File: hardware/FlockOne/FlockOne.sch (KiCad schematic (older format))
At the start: 13 parts, among them J1 Port, J2 Programming, U1 MIC5219-3.3YM5, U2 STM32F030F4P6, U3 AITHINKER-RA02

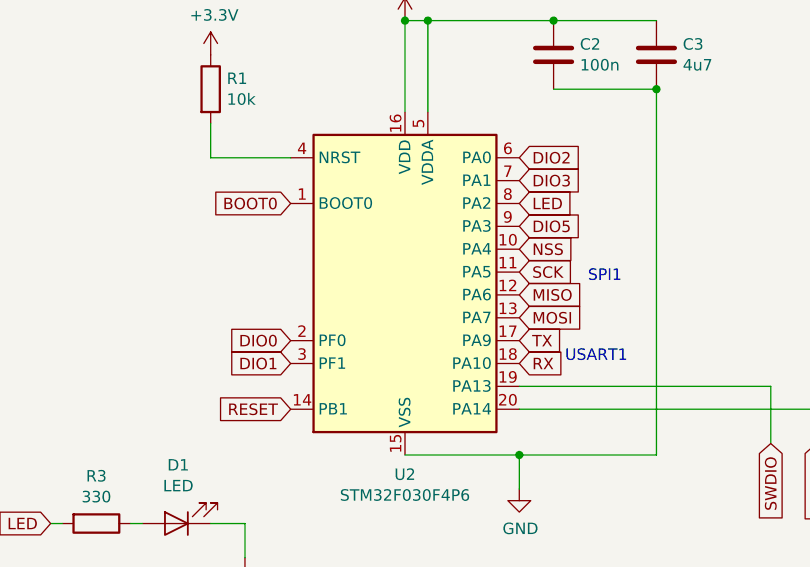
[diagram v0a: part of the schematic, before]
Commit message: Move DIO5 to HSE bypass input
This lets use use the xtal in the LoRa module as HSE rather than
using it for trimming HSI.
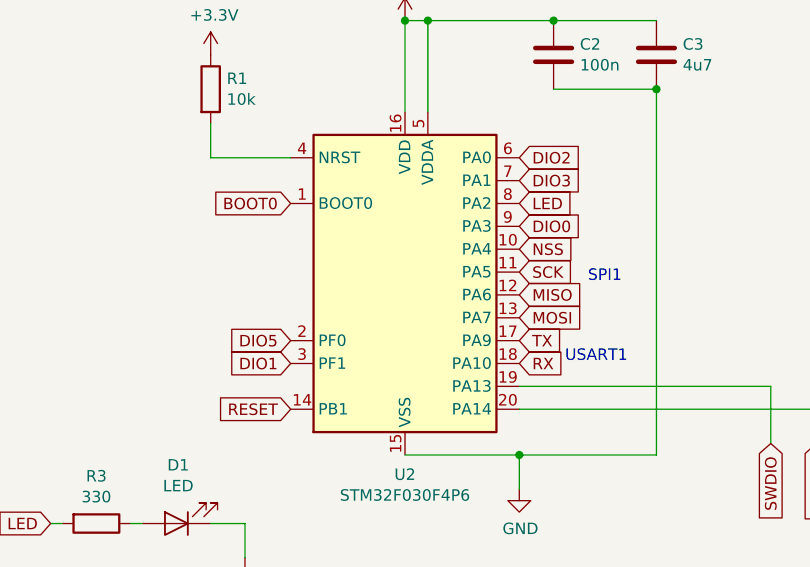
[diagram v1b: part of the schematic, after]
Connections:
- net DIO0: now also U2.9 (PA3); no longer U2.2 (PF0)
- net DIO5: now also U2.2 (PF0); no longer U2.9 (PA3)
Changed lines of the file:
@@
 EESchema Schematic File Version 4
 LIBS:FlockOne-cache
-EELAYER 26 0
+EELAYER 29 0
 EELAYER END
 $Descr A4 11693 8268
@@
 Text GLabel 6650 2500 0    50   Input ~ 0
 DIO0
-Text GLabel 3900 3050 0    50   Input ~ 0
+Text GLabel 4900 2550 2    50   Input ~ 0
 DIO0
 Text GLabel 3900 3150 0    50   Input ~ 0
@@
 Text GLabel 6650 2700 0    50   Input ~ 0
 DIO2
-Text GLabel 4900 2550 2    50   Input ~ 0
+Text GLabel 3900 3050 0    50   Input ~ 0
 DIO5
 Wire Wire Line
